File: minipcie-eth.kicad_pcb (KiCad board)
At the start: 2 copper layers, 142.7 x 47 mm, 38 parts, among them J1 UART2, J2 GPIO, J3 Micro_SD, U1 VoCore_v2, U2 si3404, U3 ap2112, U4 MPCIE-Socket, X1 SI-52003-F

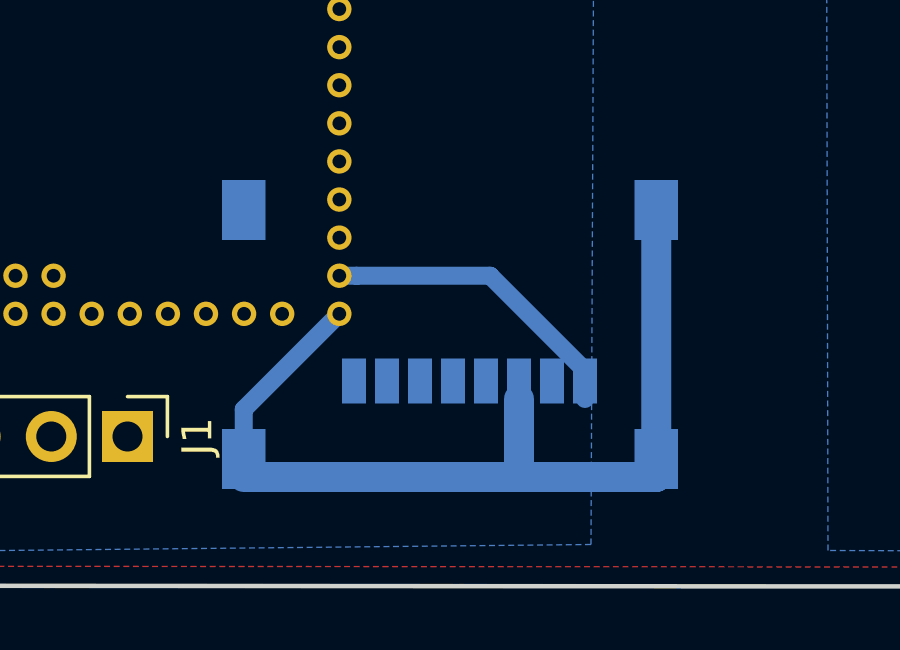
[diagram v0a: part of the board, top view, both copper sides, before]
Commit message: Migrate to KiCad 5.1 :)
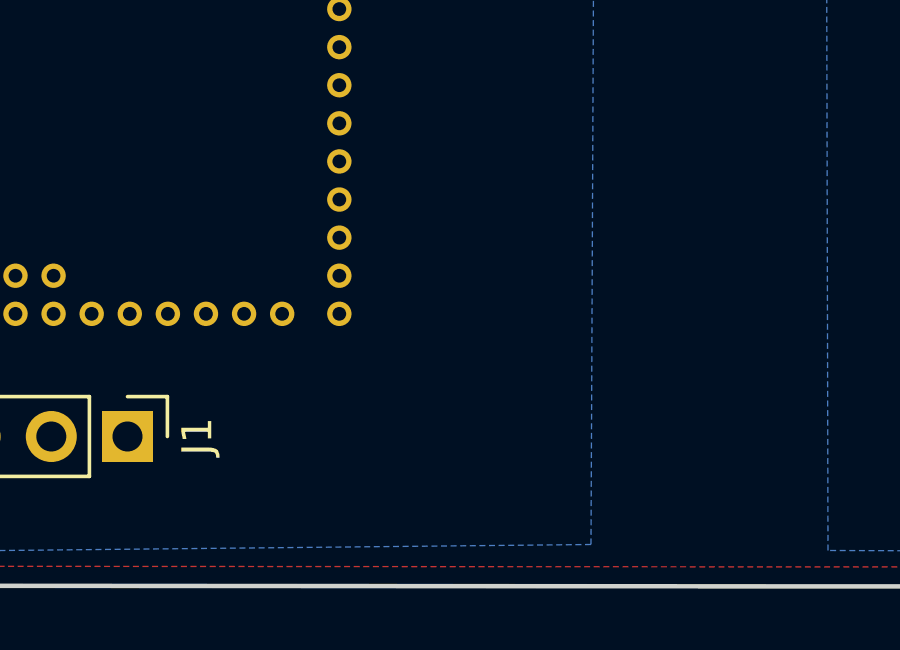
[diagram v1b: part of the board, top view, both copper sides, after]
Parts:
- removed J3: Micro_SD, KiCad/Connect.pretty:microSD_Card_Receptacle_Wuerth_693072010801
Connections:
- U1 pad 19: GND -> Net-(U1-Pad19)
- U1 pad 20: /sdcard/SD_D1 -> Net-(U1-Pad20)
- U1 pad 21: /sdcard/SD_D0 -> Net-(U1-Pad21)
- U1 pad 22: /sdcard/SD_CLK -> Net-(U1-Pad22)
- U1 pad 23: /sdcard/SD_CMD -> Net-(U1-Pad23)
- U1 pad 24: /sdcard/SD_D3 -> Net-(U1-Pad24)
- U1 pad 25: /sdcard/SD_D2 -> Net-(U1-Pad25)
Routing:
- net GND: track 85.7 -> 54.3 mm
- net /sdcard/SD_D1: track 10.4 -> 0.00 mm

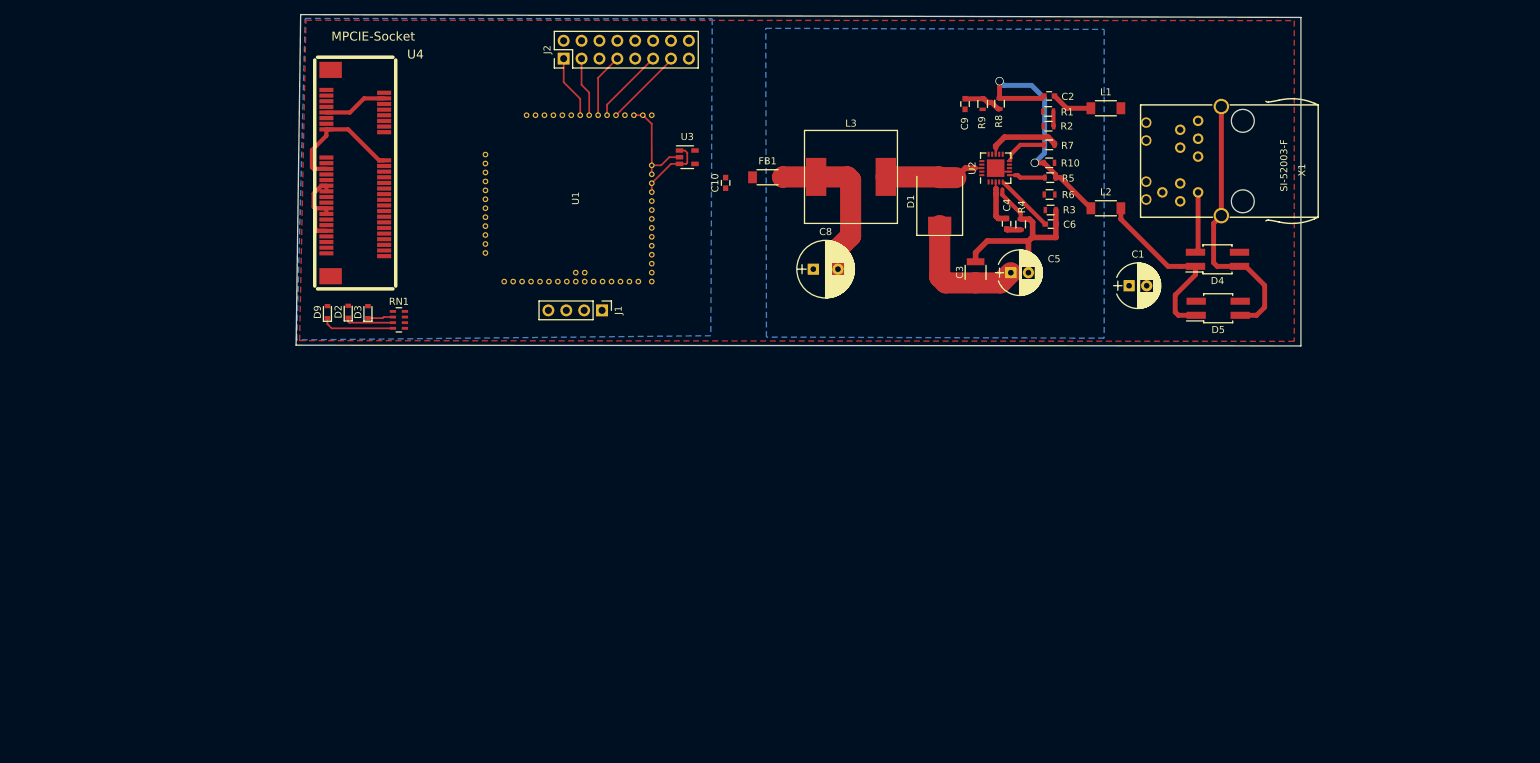
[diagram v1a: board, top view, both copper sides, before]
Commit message: Migrate to board cuts/outline with hole for the VoCore
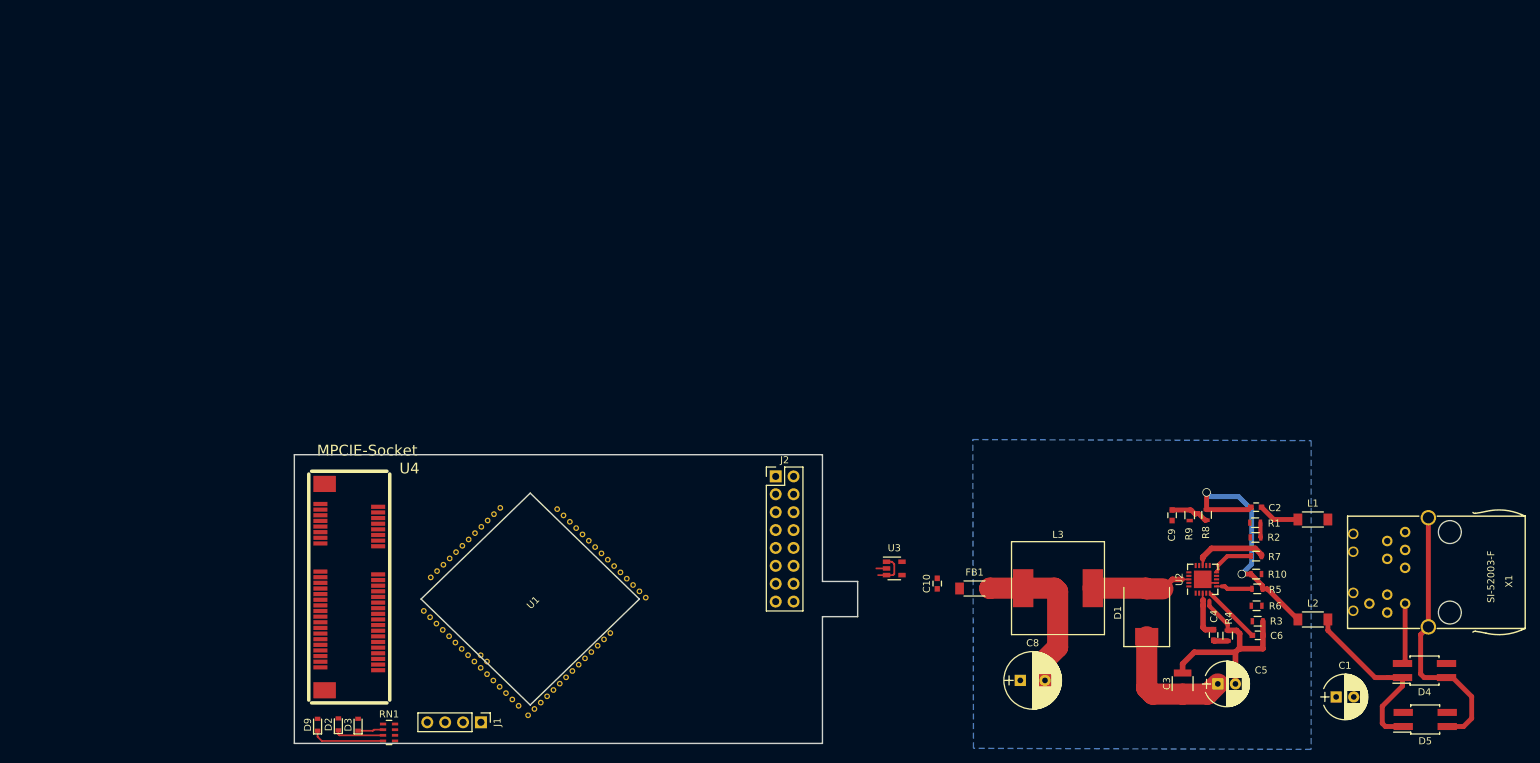
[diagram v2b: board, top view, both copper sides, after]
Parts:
- moved J2 66.5 mm to (172.5, 110.4), turned to 0 degrees
- moved D4 65.4 mm to (264.6, 137.9)
- moved L1 65.4 mm to (248.8, 116.5)
- moved R2 65.4 mm to (240.6, 119.0)
- moved C1 65.4 mm to (252.1, 141.7)
- moved C2 65.4 mm to (240.7, 114.8)
- moved C3 65.4 mm to (230.2, 139.8)
- moved C4 65.4 mm to (234.7, 132.9)
- moved C5 65.4 mm to (235.2, 139.8)
- moved C6 65.4 mm to (240.9, 132.9)
- moved C9 65.4 mm to (228.8, 115.9)
- moved D1 65.4 mm to (225.2, 129.8)
- moved D5 65.4 mm to (264.7, 144.9)
- moved L2 65.4 mm to (248.8, 130.7)
- moved L3 65.4 mm to (212.6, 126.2)
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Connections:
- J2 pad 15: Net-(J2-Pad15) -> (no net)
- J2 pad 2: Net-(J2-Pad2) -> (no net)
- J2 pad 4: Net-(J2-Pad4) -> (no net)
- RN1 pad 5: Net-(RN1-Pad5) -> (no net)
- U1 pad 11: Net-(U1-Pad11) -> (no net)
- U1 pad 12: Net-(U1-Pad12) -> (no net)
- U1 pad 13: Net-(U1-Pad13) -> (no net)
- U1 pad 14: Net-(U1-Pad14) -> (no net)
- U1 pad 15: Net-(U1-Pad15) -> (no net)
- U1 pad 16: Net-(U1-Pad16) -> (no net)
- U1 pad 17: Net-(U1-Pad17) -> (no net)
- U1 pad 18: Net-(U1-Pad18) -> (no net)
- U1 pad 19: Net-(U1-Pad19) -> (no net)
- U1 pad 2: Net-(U1-Pad2) -> (no net)
- U1 pad 20: Net-(U1-Pad20) -> (no net)
- U1 pad 21: Net-(U1-Pad21) -> (no net)
- U1 pad 22: Net-(U1-Pad22) -> (no net)
- U1 pad 23: Net-(U1-Pad23) -> (no net)
- U1 pad 24: Net-(U1-Pad24) -> (no net)
- U1 pad 25: Net-(U1-Pad25) -> (no net)
- U1 pad 26: Net-(U1-Pad26) -> (no net)
- U1 pad 3: Net-(U1-Pad3) -> (no net)
- U1 pad 33: Net-(U1-Pad33) -> (no net)
- U1 pad 36: Net-(U1-Pad36) -> (no net)
- U1 pad 4: Net-(U1-Pad4) -> (no net)
- U1 pad 48: Net-(U1-Pad48) -> (no net)
- U1 pad 52: Net-(U1-Pad52) -> (no net)
- U1 pad 53: Net-(U1-Pad53) -> (no net)
- U1 pad 54: Net-(U1-Pad54) -> (no net)
- U2 pad 11: Net-(U2-Pad11) -> (no net)
- U2 pad 12: Net-(U2-Pad12) -> (no net)
- U2 pad 14: Net-(U2-Pad14) -> (no net)
- U2 pad 15: Net-(U2-Pad15) -> (no net)
- U2 pad 16: Net-(U2-Pad16) -> (no net)
- U2 pad 17: Net-(U2-Pad17) -> (no net)
- U2 pad 2: Net-(U2-Pad2) -> (no net)
- U2 pad 20: Net-(U2-Pad20) -> (no net)
- U3 pad 4: Net-(U3-Pad4) -> (no net)
- U4 pad 1: Net-(U4-Pad1) -> (no net)
- U4 pad 11: Net-(U4-Pad11) -> (no net)
- U4 pad 13: Net-(U4-Pad13) -> (no net)
- U4 pad 14: Net-(U4-Pad14) -> (no net)
- U4 pad 17: Net-(U4-Pad17) -> (no net)
- U4 pad 19: Net-(U4-Pad19) -> (no net)
- U4 pad 23: Net-(U4-Pad23) -> (no net)
- U4 pad 25: Net-(U4-Pad25) -> (no net)
- U4 pad 28: Net-(U4-Pad28) -> (no net)
- U4 pad 3: Net-(U4-Pad3) -> (no net)
- U4 pad 30: Net-(U4-Pad30) -> (no net)
- U4 pad 31: Net-(U4-Pad31) -> (no net)
- U4 pad 32: Net-(U4-Pad32) -> (no net)
- U4 pad 33: Net-(U4-Pad33) -> (no net)
- U4 pad 46: Net-(U4-Pad46) -> (no net)
- U4 pad 48: Net-(U4-Pad48) -> (no net)
- U4 pad 5: /minipcie/GPS_PPS -> (no net)
- U4 pad 6: Net-(U4-Pad6) -> (no net)
- U4 pad 7: Net-(U4-Pad7) -> (no net)
- U4 pad 8: Net-(U4-Pad8) -> (no net)
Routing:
- net GND: track 54.3 -> 1.45 mm
- net Net-(J2-Pad13): track 11.3 -> 0.00 mm
- net Net-(J2-Pad11): track 10.7 -> 0.00 mm
- net Net-(J2-Pad7): track 9.17 -> 0.00 mm
- net Net-(J2-Pad1): track 9.01 -> 0.00 mm
- net Net-(J2-Pad3): track 8.49 -> 0.00 mm
- net +5V: track 67.6 -> 62.4 mm
- removed copper zone on B.Cu, net +3V3
- removed copper zone on F.Cu, net GND
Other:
- board size 142.7 x 47 mm -> 80 x 41 mm

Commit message: Move libs away from rescue. Re-constrained board layout since cutouts were not perpendicular (overconstrained)
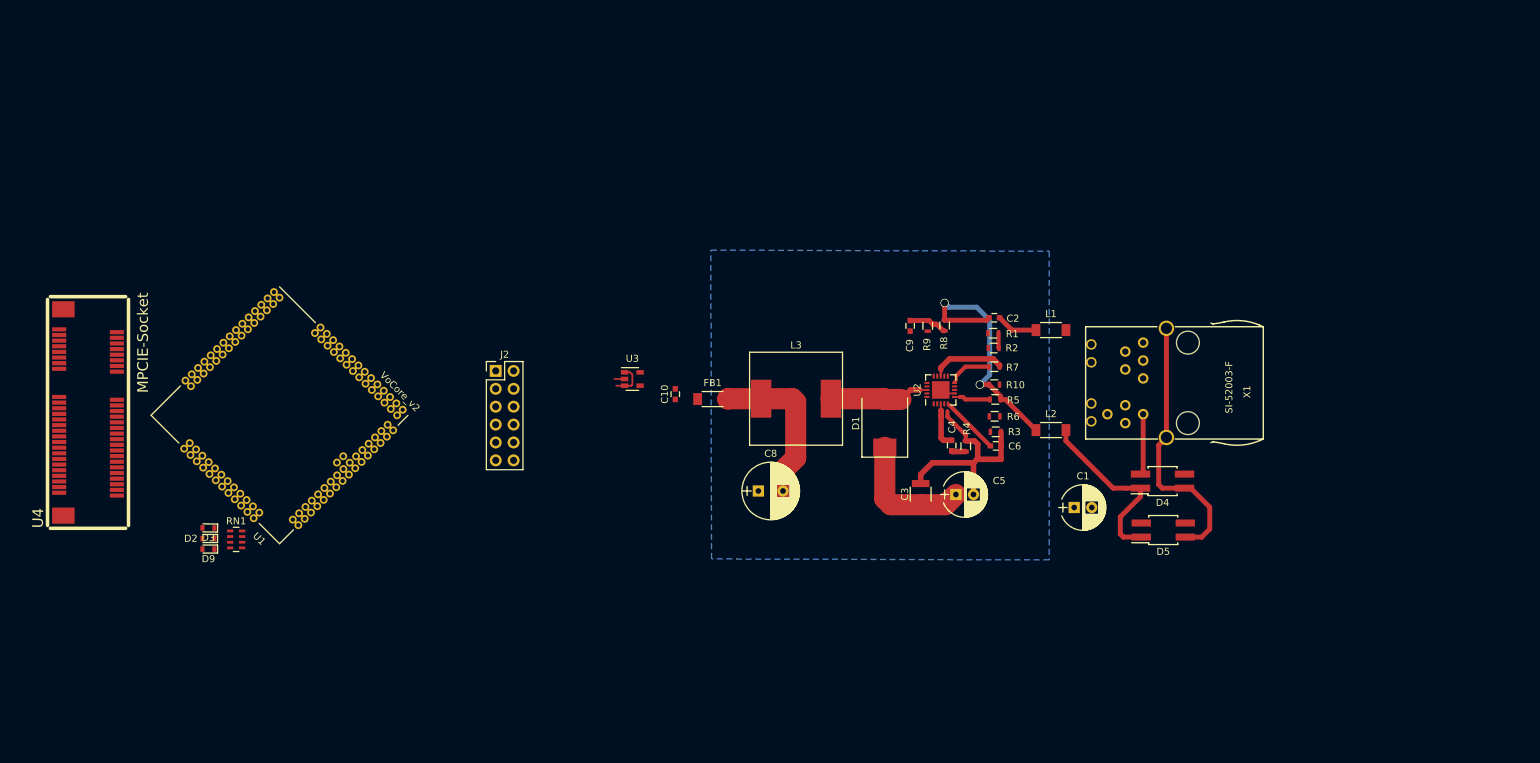
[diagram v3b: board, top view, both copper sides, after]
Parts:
- removed J1: UART2, KiCad/Pin_Headers.pretty:Pin_Header_Straight_1x04_Pitch2.54mm
- J2: value GPIO -> POE PMOD; footprint KiCad/Pin_Headers.pretty:Pin_Header_Straight_2x08_Pitch2.54mm -> Connector_PinHeader_2.54mm:PinHeader_2x06_P2.54mm_Vertical
- U1: footprint win:VoCore_v2 -> vocore2:VOCORE2
- moved C4 45.9 mm to (197.4, 106.0)
- moved D1 45.9 mm to (187.9, 102.8)
- moved L3 45.9 mm to (175.3, 99.3)
- moved R1 45.9 mm to (203.3, 90.0)
- moved R4 45.9 mm to (199.4, 106.1)
- moved U3 45.9 mm to (152.1, 96.5)
- moved C1 45.9 mm to (214.8, 114.8)
- moved C10 45.9 mm to (158.2, 98.7)
- moved C6 45.9 mm to (203.7, 106.0)
- moved D4 45.9 mm to (227.4, 111.0)
- moved R3 45.9 mm to (203.7, 104.0)
- moved R8 45.9 mm to (196.4, 89.0)
- moved C2 45.9 mm to (203.5, 87.8)
- moved C3 45.9 mm to (193.1, 112.9)
- moved C9 45.9 mm to (191.6, 89.0)
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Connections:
- net /ethernet + POE/P0RN renamed /ethernet + POE/PORN
- net /ethernet + POE/P0RP renamed /ethernet + POE/PORP
- net /ethernet + POE/P0TN renamed /ethernet + POE/POTN
- net /ethernet + POE/P0TP renamed /ethernet + POE/POTP
- J2 pad 10: GND -> Net-(J2-Pad10)
- J2 pad 11: Net-(J2-Pad11) -> GNDA
- J2 pad 12: GND -> VBUS
- J2 pad 2: (no net) -> Net-(J2-Pad2)
- J2 pad 4: (no net) -> Net-(J2-Pad4)
- J2 pad 5: GND -> GNDA
- J2 pad 6: Net-(J2-Pad6) -> VBUS
- J2 pad 8: GND -> Net-(J2-Pad8)
- J2 pad 9: GND -> Net-(J2-Pad9)
- U1 pad 13: (no net) -> Net-(U1-Pad13)
- U1 pad 14: (no net) -> Net-(U1-Pad14)
- U1 pad 15: (no net) -> Net-(U1-Pad15)
- U1 pad 16: (no net) -> Net-(U1-Pad16)
- U1 pad 17: (no net) -> Net-(U1-Pad17)
- U1 pad 18: (no net) -> Net-(U1-Pad18)
- U1 pad 19: (no net) -> Net-(U1-Pad19)
- U1 pad 2: (no net) -> Net-(U1-Pad2)
- U1 pad 20: (no net) -> Net-(U1-Pad20)
- U1 pad 21: (no net) -> Net-(U1-Pad21)
- U1 pad 22: (no net) -> Net-(U1-Pad22)
- U1 pad 23: (no net) -> Net-(U1-Pad23)
- U1 pad 24: (no net) -> Net-(U1-Pad24)
- U1 pad 25: (no net) -> Net-(U1-Pad25)
- U1 pad 26: (no net) -> Net-(U1-Pad26)
- U1 pad 3: (no net) -> Net-(U1-Pad3)
- U1 pad 33: (no net) -> Net-(U1-Pad33)
- U1 pad 34: GND -> Net-(U1-Pad34)
- U1 pad 35: GND -> Net-(U1-Pad35)
- U1 pad 36: (no net) -> Net-(U1-Pad36)
- U1 pad 37: Net-(J2-Pad13) -> Net-(U1-Pad37)
- U1 pad 38: Net-(J2-Pad11) -> Net-(U1-Pad38)
- U1 pad 39: Net-(J2-Pad7) -> Net-(U1-Pad39)
- U1 pad 4: (no net) -> Net-(U1-Pad4)
- U1 pad 40: Net-(J2-Pad3) -> Net-(U1-Pad40)
- U1 pad 41: Net-(J2-Pad1) -> Net-(U1-Pad41)
- U1 pad 44: Net-(J2-Pad6) -> Net-(U1-Pad44)
- U1 pad 48: (no net) -> Net-(U1-Pad48)
- U1 pad 52: (no net) -> Net-(U1-Pad52)
- U1 pad 53: (no net) -> Net-(U1-Pad53)
- U1 pad 54: (no net) -> Net-(U1-Pad54)
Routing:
- net Net-(D9-Pad1): track 10.4 -> 0.00 mm
- net Net-(D2-Pad1): track 6.96 -> 0.00 mm
- net Net-(D3-Pad1): track 3.61 -> 0.00 mm
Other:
- board outline removed
- net class Default: clearance 0.2 -> 0.13
- rule trace_clearance: 0.2 -> 0.13

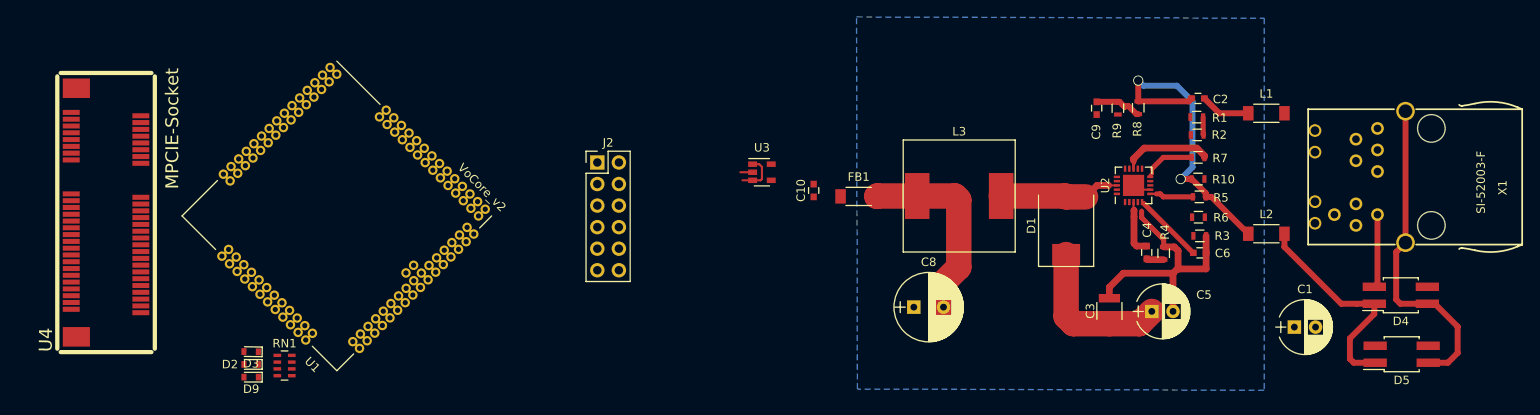
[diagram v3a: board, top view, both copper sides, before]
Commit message: Mirrored board layout to accomodate the silabs companion board
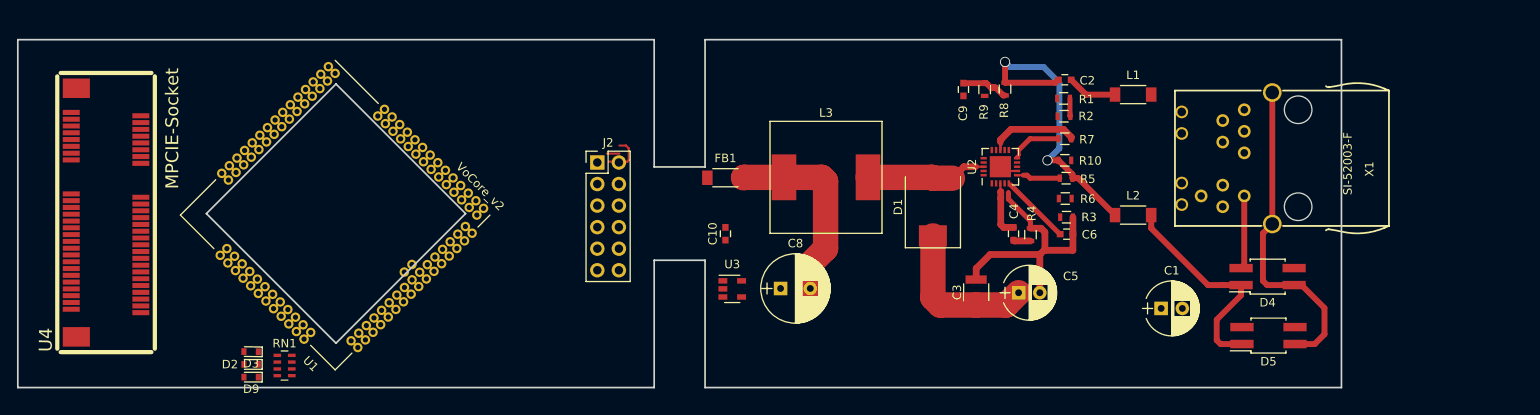
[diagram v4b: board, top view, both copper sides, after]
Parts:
- moved C3 15.9 mm to (177.3, 110.7)
- moved C5 15.9 mm to (182.3, 110.8)
- moved C9 15.9 mm to (175.8, 86.8)
- moved D4 15.9 mm to (211.7, 108.8)
- moved L1 15.9 mm to (195.8, 87.4)
- moved L2 15.9 mm to (195.8, 101.6)
- moved R2 15.9 mm to (187.7, 90.0)
- moved R5 15.9 mm to (187.9, 97.2)
- moved R6 15.9 mm to (187.8, 99.7)
- moved R9 15.9 mm to (178.3, 86.8)
- moved U2 15.9 mm to (180.2, 95.9)
- moved C1 15.9 mm to (199.2, 112.6)
- moved C2 15.9 mm to (187.8, 85.7)
- moved C4 15.9 mm to (181.8, 103.8)
- moved C6 15.9 mm to (188.0, 103.8)
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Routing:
- net +5V: track 62.4 -> 57.4 mm
- net Net-(J2-Pad2): track 0.00 -> 5.02 mm
- removed copper zone on B.Cu, net +5V
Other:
- board outline added: 156 x 41 mm
